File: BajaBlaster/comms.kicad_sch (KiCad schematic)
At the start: 7 parts, among them J501 Conn_01x06_Pin, J502 INTERBOARD, J503 Conn_01x04_Pin, U501 TCAN330

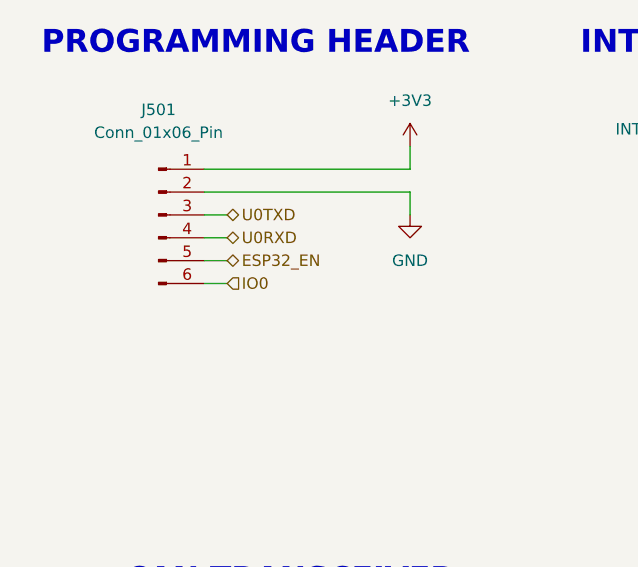
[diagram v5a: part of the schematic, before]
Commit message: passed erc with no errors just hella warnings
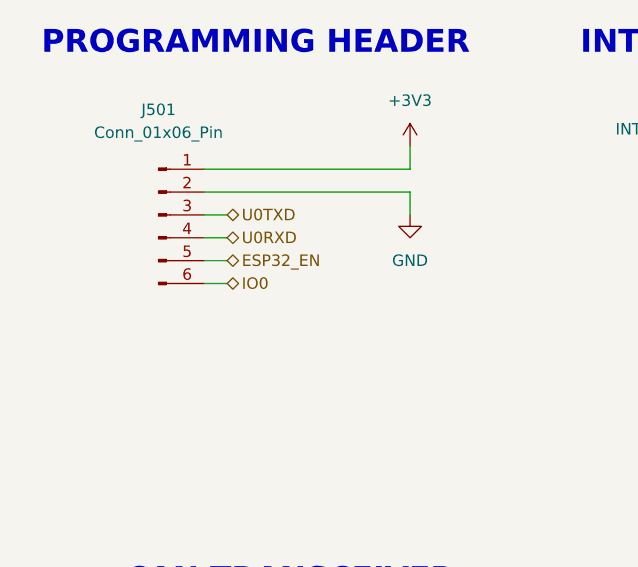
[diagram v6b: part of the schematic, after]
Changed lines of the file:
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@@
 	)
 	(hierarchical_label "IO0"
-		(shape input)
+		(shape bidirectional)
 		(at 36.83 47.625 0)
 		(effects

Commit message: working on adding footprints - about half done
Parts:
- C501: footprint (none) -> Capacitor_SMD:C_0805_2012Metric
- JP501: footprint (none) -> Jumper:SolderJumper-2_P1.3mm_Open_Pad1.0x1.5mm
- R_CAN_TERM501: footprint (none) -> Resistor_SMD:R_0805_2012Metric
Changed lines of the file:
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@@
 			)
 		)
-		(property "Footprint" ""
+		(property "Footprint" "Jumper:SolderJumper-2_P1.3mm_Open_Pad1.0x1.5mm"
 			(at 173.99 81.28 0)
 			(hide yes)
@@
 			)
 		)
-		(property "Footprint" ""
+		(property "Footprint" "Capacitor_SMD:C_0805_2012Metric"
 			(at 47.625 94.9198 0)
 			(hide yes)
@@
 			)
 		)
-		(property "Footprint" ""
+		(property "Footprint" "Resistor_SMD:R_0805_2012Metric"
 			(at 172.212 70.485 90)
 			(hide yes)

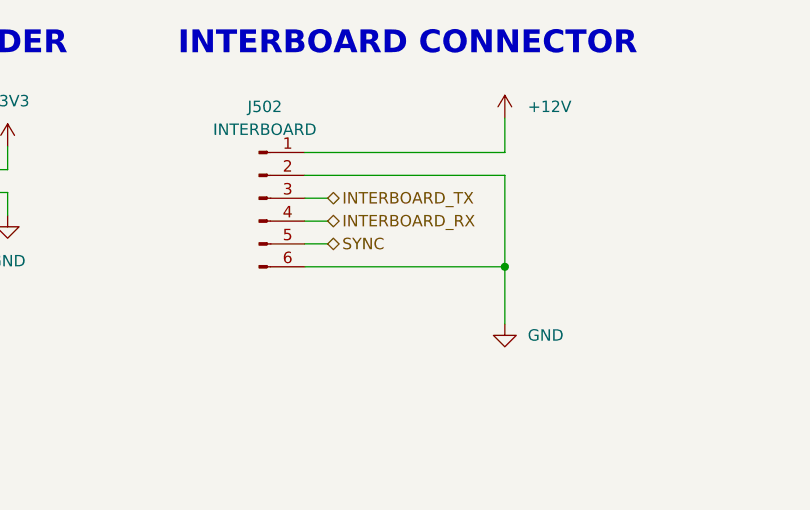
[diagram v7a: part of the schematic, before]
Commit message: added all the footprints - no errors - dont know if they are correct yet though
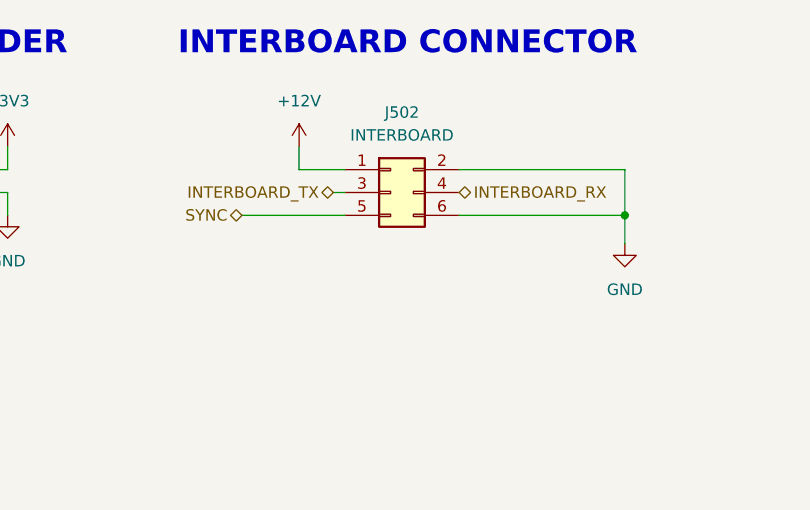
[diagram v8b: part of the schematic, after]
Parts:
- J501: footprint (none) -> Connector_PinHeader_2.54mm:PinHeader_1x06_P2.54mm_Vertical
- J502: footprint Package_DFN_QFN:QFN-20-1EP_5x5mm_P0.65mm_EP3.35x3.35mm -> Connector_Molex:Molex_Micro-Fit_3.0_43045-0600_2x03_P3.00mm_Horizontal; symbol Connector:Conn_01x06_Pin -> Connector_Generic:Conn_02x03_Odd_Even
- J503: footprint (none) -> Connector_Molex:Molex_Micro-Fit_3.0_43650-0410_1x04-1MP_P3.00mm_Horizontal
- U501: footprint (none) -> Package_SO:SOIC-8_3.9x4.9mm_P1.27mm
